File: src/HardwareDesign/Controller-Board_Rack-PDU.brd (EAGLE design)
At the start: 81.3 x 75.9 mm, 131 parts, among them IC2 RP2040, IC3 MCP6001, IC5 MIC5504-3.3YM5-TR, IC7 MP2315TSOT23-8, X1 25MHz, X2 12MHz

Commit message: finish relay board design
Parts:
- removed 3V3, 5VAC-1, 5VAC-2, 5VRMS, SW, VFB, _GND: TP, ds_passive:TP
- removed BR1: CDBHD240, 52101-101-REV-A_v16:RECTIFIER_TO-269AA
- removed C41: 10uF, ds_passive:0402
- removed C50: 1nF, ds_passive:0402
- removed D1: MBR0520LT1G, Diodes:SOD-123
- added 12VFB, 3V3DC, GND-3, GND-5, SW3, SW5, VFB3, VFB5: TP, ds_passive:TP
- added C45, C46, C57: 22uF, ds_passive:C1206
- added L3: 4.2uH, ds_passive:SRR5228A
- added R32: 7.5K, ds_passive:0402
- added R41: 10R, ds_passive:0402
- added R42: 33K, ds_passive:0402
- added R43: 40.2K, ds_passive:0402
- added R44: 12.7K, ds_passive:0402
- added R45: 100K, ds_passive:0402
- added R46, R47: 0R, ds_passive:0402
- added R48, R49: 4.7K, ds_passive:0402
- added R50: 10K, ds_passive:0402
- added RESET: B3U-1000P, 52101-101-REV-A_v16:SWITCH-OMRON_B3U-1000P
- C1, C10, C11, C12, C13, C14, C15, C16, C17, C18, C19, C2, C20, C21, C22, C23, C24, C25, C28, C29, C3, C30, C31, C32, C33, C34, C35, C37, C38, C39, C4, C55, C56, C6, C7, C8, C9, R5, R6: device ds_passive:0402 -> ds_passive:C0402
- C36: value 10uF -> 100nF
- C43: value 1000uF 25V -> 33pF; device Capacitor:CAPPRD508W65D1000H1100B -> ds_passive:0402
- C44: value 1000uF 25V -> 22uF; device Capacitor:CAPPRD508W65D1000H1100B -> ds_passive:C1206
- C47: device ds_passive:100UF-16V -> ds_passive:C1206
- C5: device ds_passive:1206 -> ds_passive:C1206
- C53: value 47uF -> 22uF; device ds_passive:100UF-16V -> ds_passive:C1206
- IC5: value MIC5504-3.3YM5-TR -> MP2315S; device ds_ic_vreg:SOT23-5 -> ds_ic_vreg:SOT65P280X110-8N
- IC7: value MP2315TSOT23-8 -> MP2315S
- L2: value 5.5uH -> 4.9uH
- R29: value (none) -> 100K; device ds_passive:1206 -> ds_passive:0402
- R30: value (none) -> 499K; device ds_passive:1206 -> ds_passive:0402
- R31: value 100K -> 499K
- R33: value 75K -> 9.09K
- R34: value 20R -> 10R
- moved GND 43.2 mm to (77.4, 35.8), turned to 270 degrees
- moved R30 41.7 mm to (29.8, 14.1), turned to 270 degrees
- moved C53 27.5 mm to (34.5, 39.7), turned to 0 degrees
- moved C43 26.8 mm to (21.0, 12.9), turned to 0 degrees
- moved L2 23.6 mm to (28.8, 41.6), turned to 90 degrees
- moved C42 21.9 mm to (23.9, 21.6), turned to 90 degrees
- moved C51 21.7 mm to (23.9, 38.6), turned to 90 degrees
- moved R34 21.6 mm to (26.0, 37.9)
- moved R29 20.1 mm to (29.3, 30.3)
- moved C40 19.3 mm to (22.6, 17.5), turned to 90 degrees
- moved C49 18.6 mm to (23.9, 35.3)
- moved C48 18.4 mm to (30.8, 35.2), turned to 90 degrees
- moved IC5 18.4 mm to (26.6, 17.2), turned to 180 degrees
- moved IC7 15.1 mm to (27.9, 34.9), turned to 180 degrees
- moved R31 14.0 mm to (30.7, 31.5), turned to 270 degrees
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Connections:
- removed net 12_VFB: IC2.39, J1.3
- removed net 5VAC1: 5VAC-1.TP, BR1.AC1
- removed net 5VAC2: 5VAC-2.TP, BR1.AC2
- removed net 5VRMS: 5VRMS.TP, BR1.+, C43.1, C44.1, C47.1, C48.1, IC7.2, R29.1, R31.1
- removed net IAC: IC2.40, J1.4
- removed net N$27: J2.12
- removed net N$28: J2.10
- removed net N$29: J2.8
- removed net N$30: J2.6
- removed net N$32: C50.1, IC7.1, R33.1
- new net +12V: C36.1, C44.1, C45.1, C48.1, IC5.2, IC7.2, J1.14, R30.1, R31.1, R48.2
- new net I_MEA/TX: IC2.40, J1.4, R46.1
- new net N$11: IC5.5, R41.2
- new net N$12: IC5.1, R32.1, R45.2
- new net N$13: IC7.1, R29.2, R33.1
- new net N$16: C49.1, IC7.7, R29.1
- new net N$17: IC2.26, R50.2, RESET.1
- new net N$20: IC5.8, R42.1
- new net N$21: C42.2, IC5.3, L3.1, SW3.TP
- new net N$22: C42.1, R41.1
- new net N$24: C43.2, R42.2, R43.2, R44.1, VFB3.TP
- new net N$26: IC5.6, R30.2
- new net V_MEA/RX: IC2.39, J1.3, R47.1
- net +3V3: now also 3V3DC.TP, C43.1, C47.1, C57.1, L3.2, R43.1, R50.1; no longer 3V3.TP, C41.1, C42.1, IC5.5
- net +5V: now also C46.1; no longer C36.1, C40.1, D1.C, IC5.1, IC5.3
- net GND: now also C45.2, C46.2, C57.2, GND-3.TP, GND-5.TP, IC5.4, R32.2, R44.2, R49.1, RESET.2; no longer BR1.-, C41.2, C42.2, C43.2, C50.2, IC5.2, J1.14, R30.2, _GND.TP
- net N$31: now also C40.1, IC5.7, R45.1; no longer C49.1, IC7.7
- net N$35: now also SW5.TP; no longer SW.TP
- net N$37: now also VFB5.TP; no longer VFB.TP
- net PWR_DETECT: now also 12VFB.TP, R48.1, R49.2; no longer R29.2, R30.1
- net UART0_RX: now also R47.2
- net UART0_TX: now also R46.2
- net VBUS: no longer D1.A
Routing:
- net 5VRMS: track 263.4 -> 0.00 mm, vias 14 -> 0
- net GND: track 893.4 -> 728.2 mm, vias 108 -> 87
- net +5V: track 214.5 -> 108.7 mm, vias 2 -> 0
- net +12V: track 0.00 -> 98.4 mm, vias 0 -> 3
- net I_MEA/TX: track 0.00 -> 94.0 mm, vias 0 -> 2
- net V_MEA/RX: track 0.00 -> 86.4 mm, vias 0 -> 2
- net 5VAC2: track 69.4 -> 0.00 mm, vias 1 -> 0
- net 5VAC1: track 62.1 -> 0.00 mm, vias 1 -> 0
- net N$17: track 0.00 -> 60.9 mm, vias 1 -> 2
- net +3V3: track 332.9 -> 380.2 mm, vias 6 -> 7
- net IAC: track 45.8 -> 0.00 mm, vias 2 -> 0
- net 12_VFB: track 39.9 -> 0.00 mm, vias 2 -> 0
- net N$21: track 0.00 -> 37.5 mm
- net VBUS: track 60.3 -> 26.4 mm, vias 3 -> 2
- net UART0_RX: track 21.1 -> 36.3 mm
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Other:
- outline, holes or cut-outs redrawn

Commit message: first order send to JLCPCB
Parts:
- C44, C45: value 22uF -> CL31A226KAHNNNE - 22uF 25V
- C46, C47, C53, C57: value 22uF -> CL31A226KPHNNNE - 22uF - 10V
- ESD1: value (none) -> SP0503BAHTG-ES
- IC1: value (none) -> W5500
- IC3: value MCP6001 -> MCP6001AIDBVRG
- IC4: value (none) -> W25Q128JVPIQ
- IC6: value (none) -> CAT24C256HU4IGT3
- IC7: value MP2315S -> MP2315GJ-Z
- IC8: value (none) -> MCP23S18-E/MJ
- R38: value 742C083103JP -> 4D03WGJ0332T5E
- RESET, USB_BOOT: value B3U-1000P -> B3U-1000P-B
- USBC: value 629722000214 -> USB-TYPE-C-018
- X1: value 25MHz -> RL250001791
- X2: value 12MHz -> SX3M12.000B10F20TNN
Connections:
- removed net N$10: IC8.1
- removed net N$77: IC8.24
- removed net N$78: IC8.2
- removed net N$79: IC8.3
- removed net N$80: IC8.4
- removed net N$81: IC8.5
- removed net N$82: IC8.6
- removed net N$83: IC8.7

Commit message: change X1, X2 because of shortage
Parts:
- X1: value RL250001791 -> XC53M4-25.000-F18NJDTL
- X2: value SX3M12.000B10F20TNN -> 5TJ412000UYGBC
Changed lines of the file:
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@@
 <attribute name="NAME" x="74.18" y="34.06" size="1.016" layer="25" rot="R270" align="center-left"/>
 </element>
-<element name="X1" library="ds_passive" package="OSCCC500X320X130" package3d_urn="urn:adsk.eagle:package:16378248/1" value="RL250001791" x="46.605" y="43.06" smashed="yes" rot="R90">
+<element name="X1" library="ds_passive" package="OSCCC500X320X130" package3d_urn="urn:adsk.eagle:package:16378248/1" value="XC53M4-25.000-F18NJDTL " x="46.605" y="43.06" smashed="yes" rot="R90">
 <attribute name="NAME" x="44.0791" y="43.06" size="1.27" layer="25" rot="R90" align="bottom-center"/>
 <attribute name="VALUE" x="49.1309" y="43.06" size="1.27" layer="27" rot="R90" align="top-center"/>
 </element>
-<element name="X2" library="ds_passive" package="OSCCC500X320X130" package3d_urn="urn:adsk.eagle:package:16378248/1" value="SX3M12.000B10F20TNN" x="54.476" y="59.11" smashed="yes" rot="R180">
+<element name="X2" library="ds_passive" package="OSCCC500X320X130" package3d_urn="urn:adsk.eagle:package:16378248/1" value="5TJ412000UYGBC " x="54.476" y="59.11" smashed="yes" rot="R180">
 <attribute name="NAME" x="57.7585" y="58.8372" size="1.27" layer="25" rot="R270" align="bottom-center"/>
 <attribute name="VALUE" x="54.476" y="61.6359" size="1.27" layer="27" rot="R180" align="top-center"/>

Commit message: update documentation
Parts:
- X1: value XC53M4-25.000-F18NJDTL -> XC53M4-25.000-F18NJDTL
- X2: value 5TJ412000UYGBC -> K5A1200015304P
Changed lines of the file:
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@@
 <attribute name="NAME" x="74.18" y="34.06" size="1.016" layer="25" rot="R270" align="center-left"/>
 </element>
-<element name="X1" library="ds_passive" package="OSCCC500X320X130" package3d_urn="urn:adsk.eagle:package:16378248/1" value="XC53M4-25.000-F18NJDTL " x="46.605" y="43.06" smashed="yes" rot="R90">
+<element name="X1" library="ds_passive" package="OSCCC500X320X130" package3d_urn="urn:adsk.eagle:package:16378248/1" value="XC53M4-25.000-F18NJDTL" x="46.605" y="43.06" smashed="yes" rot="R90">
 <attribute name="NAME" x="44.0791" y="43.06" size="1.27" layer="25" rot="R90" align="bottom-center"/>
 <attribute name="VALUE" x="49.1309" y="43.06" size="1.27" layer="27" rot="R90" align="top-center"/>
 </element>
-<element name="X2" library="ds_passive" package="OSCCC500X320X130" package3d_urn="urn:adsk.eagle:package:16378248/1" value="5TJ412000UYGBC " x="54.476" y="59.11" smashed="yes" rot="R180">
+<element name="X2" library="ds_passive" package="OSCCC500X320X130" package3d_urn="urn:adsk.eagle:package:16378248/1" value="K5A1200015304P" x="54.476" y="59.11" smashed="yes" rot="R180">
 <attribute name="NAME" x="57.7585" y="58.8372" size="1.27" layer="25" rot="R270" align="bottom-center"/>
 <attribute name="VALUE" x="54.476" y="61.6359" size="1.27" layer="27" rot="R180" align="top-center"/>

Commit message: correct wrong divider resistor values
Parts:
- R25: value 5.6K -> 10K
- R48: value 4.7K -> 100K
- R49: value 4.7K -> 10K
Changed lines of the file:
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@@
 <attribute name="VALUE" x="73.357" y="13.827" size="1.016" layer="27" rot="R90"/>
 </element>
-<element name="R25" library="ds_passive" library_urn="urn:adsk.eagle:library:46685041" package="0402" package3d_urn="urn:adsk.eagle:package:46683744/2" value="5.6K" x="69.1914" y="15.3764" smashed="yes" rot="R180">
+<element name="R25" library="ds_passive" library_urn="urn:adsk.eagle:library:46685041" package="0402" package3d_urn="urn:adsk.eagle:package:46683744/2" value="10K" x="69.1914" y="15.3764" smashed="yes" rot="R180">
 <attribute name="NAME" x="66.9736" y="17.4586" size="1.016" layer="25"/>
 <attribute name="VALUE" x="69.8264" y="17.2814" size="1.016" layer="27" rot="R180"/>
@@
 <attribute name="VALUE" x="62.165" y="68.945" size="1.016" layer="27"/>
 </element>
-<element name="R48" library="ds_passive" package="0402" package3d_urn="urn:adsk.eagle:package:46683744/2" value="4.7K" x="37" y="52.15" smashed="yes" rot="R180">
+<element name="R48" library="ds_passive" package="0402" package3d_urn="urn:adsk.eagle:package:46683744/2" value="100K" x="37" y="52.15" smashed="yes" rot="R180">
 <attribute name="NAME" x="37.635" y="51.515" size="1.016" layer="25" rot="R180"/>
 <attribute name="VALUE" x="37.635" y="54.055" size="1.016" layer="27" rot="R180"/>
 </element>
-<element name="R49" library="ds_passive" package="0402" package3d_urn="urn:adsk.eagle:package:46683744/2" value="4.7K" x="40.1" y="52.15" smashed="yes" rot="R180">
+<element name="R49" library="ds_passive" package="0402" package3d_urn="urn:adsk.eagle:package:46683744/2" value="10K" x="40.1" y="52.15" smashed="yes" rot="R180">
 <attribute name="NAME" x="40.735" y="51.515" size="1.016" layer="25" rot="R180"/>
 <attribute name="VALUE" x="40.735" y="54.055" size="1.016" layer="27" rot="R180"/>

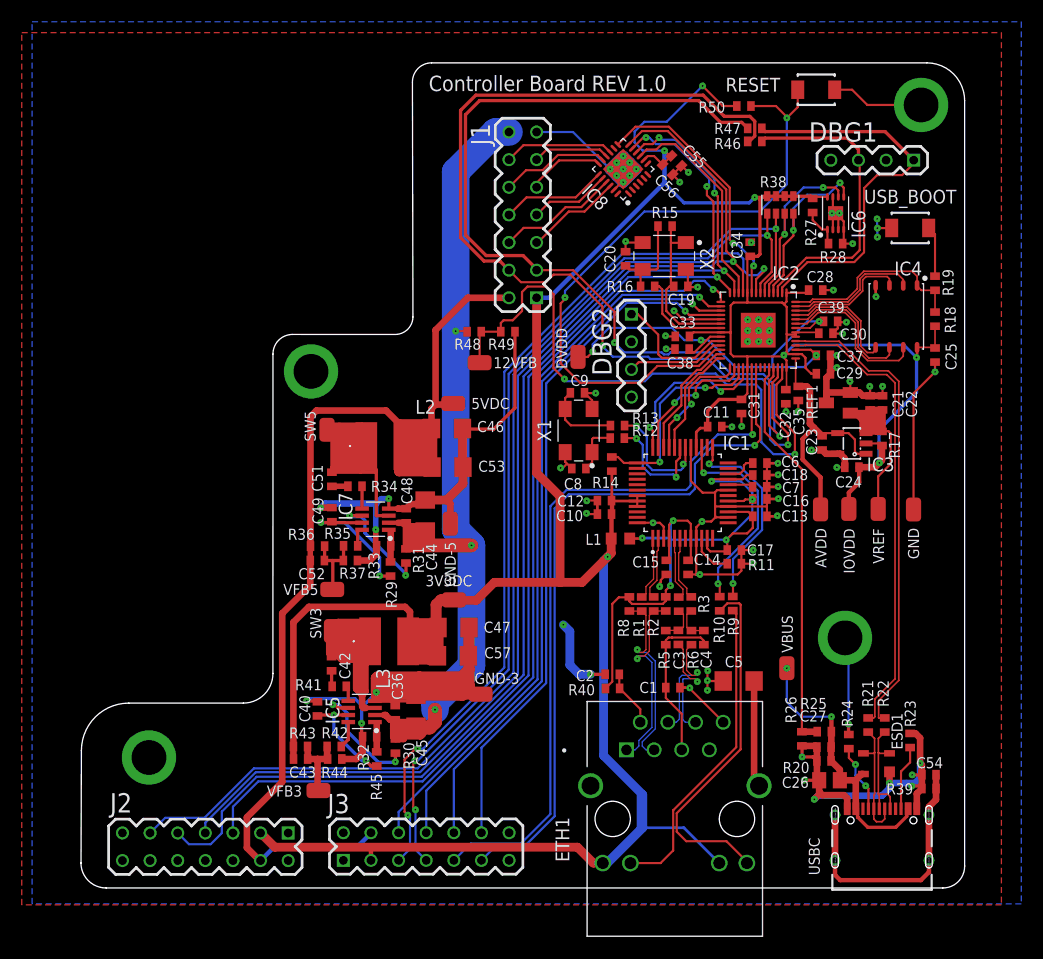
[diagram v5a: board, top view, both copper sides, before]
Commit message: add DiffPairCheck to repo. Update Controller-boart to rev1.1
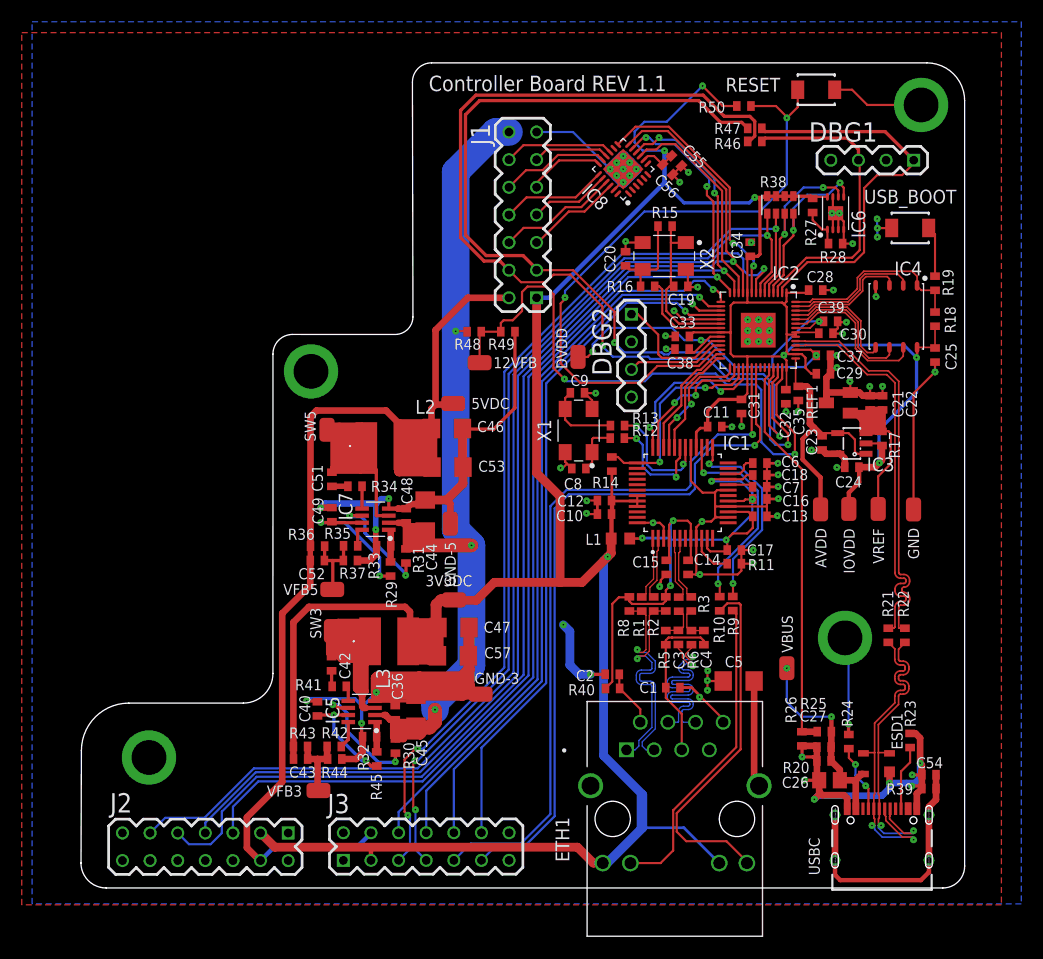
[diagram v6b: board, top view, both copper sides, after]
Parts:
- moved R21 8.45 mm to (75.1, 24.2)
- moved R22 8.45 mm to (76.6, 24.2)
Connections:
- net RDC_N renamed RDC_RD_N
- net RDC_P renamed RDC_RD_P
- net RP_USBD_N renamed USB_DP_N
- net RP_USBD_P renamed USB_DP_P
- net RX_N renamed RX_RD_N
- net RX_P renamed RX_RD_P
- net TX_N renamed TX_TD_N
- net TX_P renamed TX_TD_P
- net USBD_N renamed DP_N
- net USBD_P renamed DP_P
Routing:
- net DP_N: track 11.5 -> 30.7 mm, vias 0 -> 2
- net DP_P: track 10.7 -> 29.5 mm, vias 0 -> 2
- net RD_P: track 11.0 -> 18.4 mm
- net RD_N: track 11.1 -> 18.4 mm
- net USB_DP_P: track 43.3 -> 36.1 mm
- net VBUS: track 26.4 -> 19.6 mm
- net USB_DP_N: track 42.7 -> 36.1 mm
- net GND: track 728.2 -> 731.6 mm
- net TD_N: track 17.8 -> 20.0 mm
- net TD_P: track 17.8 -> 20.0 mm
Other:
- board text added: "Controller Board REV 1.1"
- board text removed: "Controller Board REV 1.0"
